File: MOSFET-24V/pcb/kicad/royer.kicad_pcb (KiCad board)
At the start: 2 copper layers, 40.6 x 59.7 mm, 26 parts, among them J1 Screw_Terminal_1x04, Q1 IRFB4410, Q2 IRFD110, Q3 IRFD110, Q4 IRFB4410

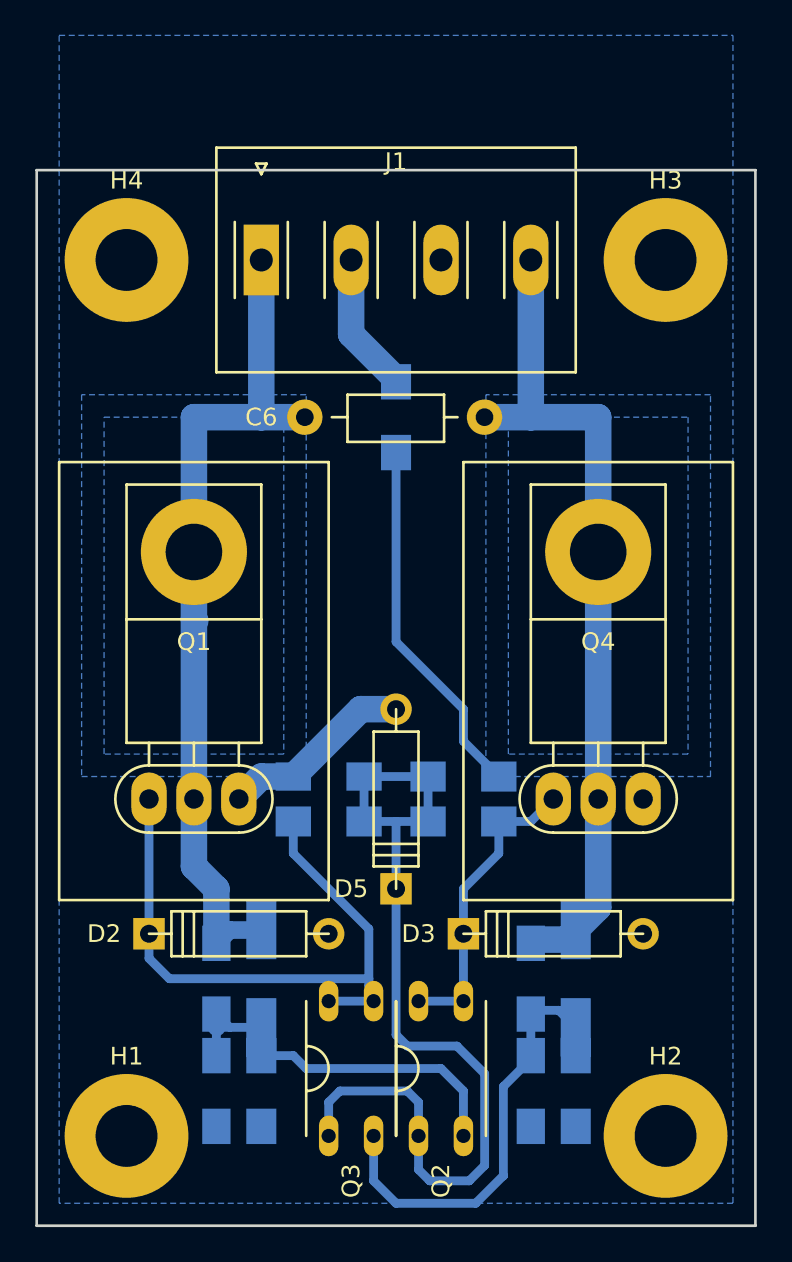
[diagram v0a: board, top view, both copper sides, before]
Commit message: pcb fill layer not rebuild after hole repositioned. It is now corrected and top GND layer is added. Sent to production
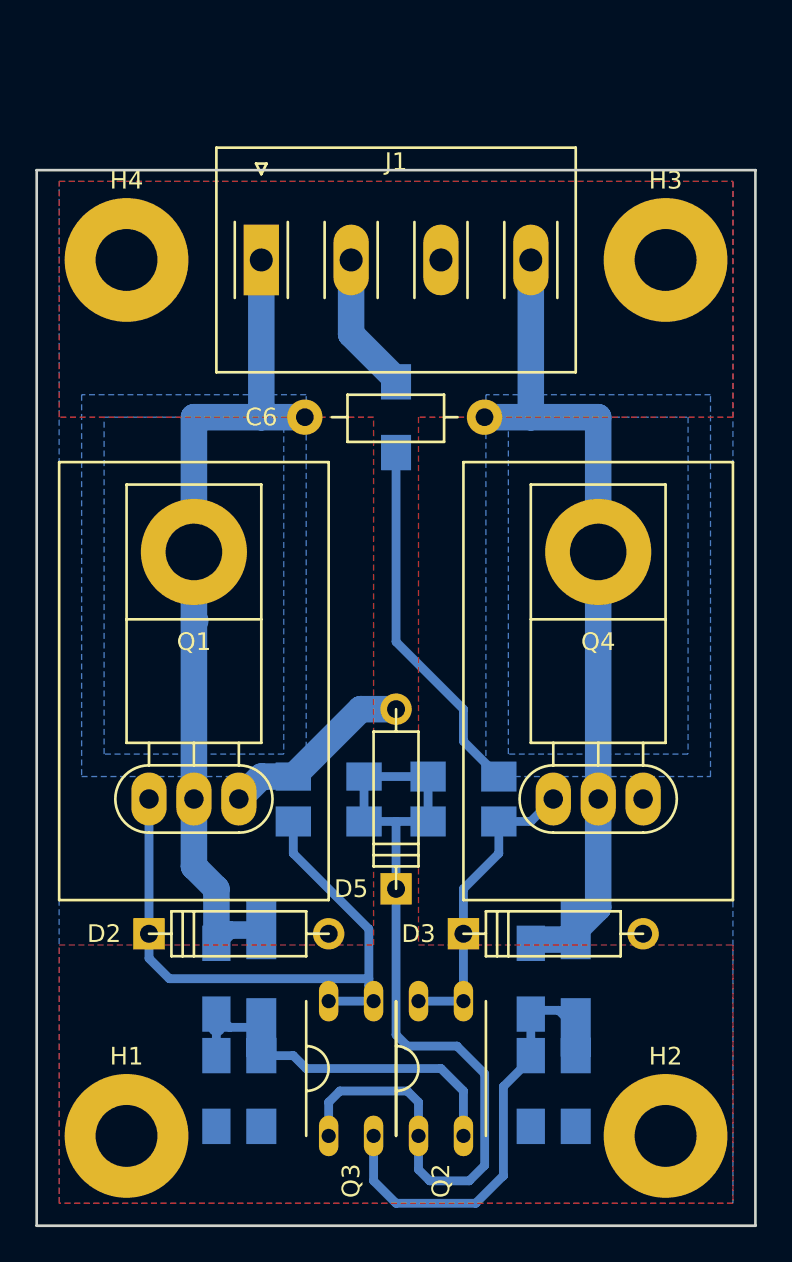
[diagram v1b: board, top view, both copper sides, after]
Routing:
- added copper zone on F.Cu, net GND
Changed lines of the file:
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@@
   (general
     (links 48)
-    (no_connects 1)
+    (no_connects 0)
     (area 142.010001 68.42 211.685 145.575001)
     (thickness 1.6)
@@
     (polygon
       (pts
-        (xy 196.85 137.16) (xy 158.75 137.16) (xy 158.75 71.12) (xy 196.85 71.12)
+        (xy 196.85 137.16) (xy 158.75 137.16) (xy 158.75 79.375) (xy 196.85 79.375)
       )
     )
@@
       )
     )
+  )
+  (zone (net 1) (net_name GND) (layer F.Cu) (hatch edge 0.508)
+    (connect_pads (clearance 0.7))
+    (min_thickness 0.254)
+    (fill yes (arc_segments 16) (thermal_gap 0.508) (thermal_bridge_width 0.508))
+    (polygon
+      (pts
+        (xy 158.75 79.375) (xy 196.85 79.375) (xy 196.85 92.71) (xy 179.07 92.71) (xy 179.07 122.555)
+        (xy 196.85 122.555) (xy 196.85 137.16) (xy 158.75 137.16) (xy 158.75 122.555) (xy 176.53 122.555)
+        (xy 176.53 92.71) (xy 158.75 92.71)
+      )
+    )

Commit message: Change from 10nF/10nF to 22nF/10nF capacitive divider
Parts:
- C1, C4: value 47nF -> 22nF
- C2, C3: value 47nF -> 10nF
- C5: value 47nF -> 470nF
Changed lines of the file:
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@@
     (links 48)
     (no_connects 0)
-    (area 142.010001 68.42 211.685 145.575001)
+    (area 157.404999 78.664999 198.195001 138.505001)
     (thickness 1.6)
     (drawings 8)
@@
       (effects (font (size 1 1) (thickness 0.15)) (justify mirror))
     )
-    (fp_text value 47nF (at 1.27 1.905 180) (layer B.Fab)
+    (fp_text value 470nF (at 1.27 1.905 180) (layer B.Fab)
       (effects (font (size 1 1) (thickness 0.15)) (justify mirror))
     )
@@
       (effects (font (size 1 1) (thickness 0.15)) (justify mirror))
     )
-    (fp_text value 47nF (at 0 -1.905 90) (layer B.Fab)
+    (fp_text value 22nF (at 0 -1.905 90) (layer B.Fab)
       (effects (font (size 1 1) (thickness 0.15)) (justify mirror))
     )
@@
       (effects (font (size 1 1) (thickness 0.15)) (justify mirror))
     )
-    (fp_text value 47nF (at -2.54 1.905 270) (layer B.Fab)
+    (fp_text value 10nF (at -2.54 1.905 270) (layer B.Fab)
       (effects (font (size 1 1) (thickness 0.15)) (justify mirror))
     )
@@
       (effects (font (size 1 1) (thickness 0.15)) (justify mirror))
     )
-    (fp_text value 47nF (at 0 1.905 270) (layer B.Fab)
+    (fp_text value 10nF (at 0 1.905 270) (layer B.Fab)
       (effects (font (size 1 1) (thickness 0.15)) (justify mirror))
     )
@@
       (effects (font (size 1 1) (thickness 0.15)) (justify mirror))
     )
-    (fp_text value 47nF (at -0.2108 -1.905 90) (layer B.Fab)
-      (effects (font (size 1 1) (thickness 0.15)) (justify mirror))
-    )
+    (fp_text value 22nF (at -0.2108 -1.905 90) (layer B.Fab)
+      (effects (font (size 1 1) (thickness 0.15)) (justify mirror))
+    )

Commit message: revert back to 10nF
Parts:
- C1, C4: value 22nF -> 10nF
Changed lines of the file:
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@@
       (effects (font (size 1 1) (thickness 0.15)) (justify mirror))
     )
-    (fp_text value 22nF (at 0 -1.905 90) (layer B.Fab)
+    (fp_text value 10nF (at 0 -1.905 90) (layer B.Fab)
       (effects (font (size 1 1) (thickness 0.15)) (justify mirror))
     )
@@
       (effects (font (size 1 1) (thickness 0.15)) (justify mirror))
     )
-    (fp_text value 22nF (at -0.2108 -1.905 90) (layer B.Fab)
-      (effects (font (size 1 1) (thickness 0.15)) (justify mirror))
-    )
+    (fp_text value 10nF (at -0.2108 -1.905 90) (layer B.Fab)
+      (effects (font (size 1 1) (thickness 0.15)) (justify mirror))
+    )
